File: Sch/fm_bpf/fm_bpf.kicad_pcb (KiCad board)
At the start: 2 copper layers, 28 parts, among them CN1 SMA_Edge, CN2 SMA_Edge, J1 JP2, U1 LP5907_SOT-23, U2 PSA4-5043+

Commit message: PCB layout in progress
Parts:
- removed J1: JP2, adc_lib:M20-9980245
- added W1: TEST_1P, adc_lib:68000-401HLF, F.Cu at (147.2, 92.5)
- added W2: TEST_1P, adc_lib:68000-401HLF, F.Cu at (144.4, 96.6)
- moved R2 8.09 mm to (143.7, 90.4), turned to 180 degrees
- moved U1 7.90 mm to (141.6, 92.5)
- moved C4 7.73 mm to (139.4, 94.4)
- moved C6 5.51 mm to (139.4, 95.6)
- moved L3 5.48 mm to (140.1, 97.9)
- moved C1 5.30 mm to (144.3, 92.8), turned to 90 degrees
- moved R1 5.07 mm to (138.4, 97.7)
- moved L4 4.74 mm to (140.0, 101.9)
- moved C8 4.55 mm to (139.3, 99.9)
- moved C13 3.36 mm to (150.1, 101.5)
- moved L7 2.01 mm to (149.0, 102.6)
- moved C12 1.84 mm to (147.1, 103.3)
- moved C14 1.72 mm to (151.8, 103.2)
- moved L6 1.54 mm to (145.9, 103.3)
- moved CN2 1.45 mm to (156.7, 102.6)
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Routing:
- net +5V: track 0.00 -> 13.3 mm
- net Net-(C12-Pad2): track 0.00 -> 4.99 mm
- net Net-(C13-Pad1): track 0.00 -> 4.41 mm
- net Net-(C4-Pad1): track 0.00 -> 4.23 mm
- net Net-(C5-Pad2): track 0.00 -> 2.97 mm
- net Net-(C8-Pad1): track 0.00 -> 2.35 mm
- net Net-(C14-Pad2): track 0.00 -> 1.66 mm
- net Net-(R2-Pad2): track 0.00 -> 1.17 mm
- net Net-(C10-Pad1): track 0.00 -> 1.09 mm
- net Net-(C3-Pad1): track 0.00 -> 1.03 mm
- net Net-(C11-Pad2): track 0.00 -> 1.00 mm
- net Net-(C7-Pad2): track 0.00 -> 0.88 mm
- added copper zone on F.Cu, net +5V
- added copper zone on B.Cu, net GND
- added copper zone on F.Cu, net GND
- added copper zone on F.Cu, net Net-(C4-Pad1)
- added copper zone on F.Cu, net Net-(C8-Pad1)

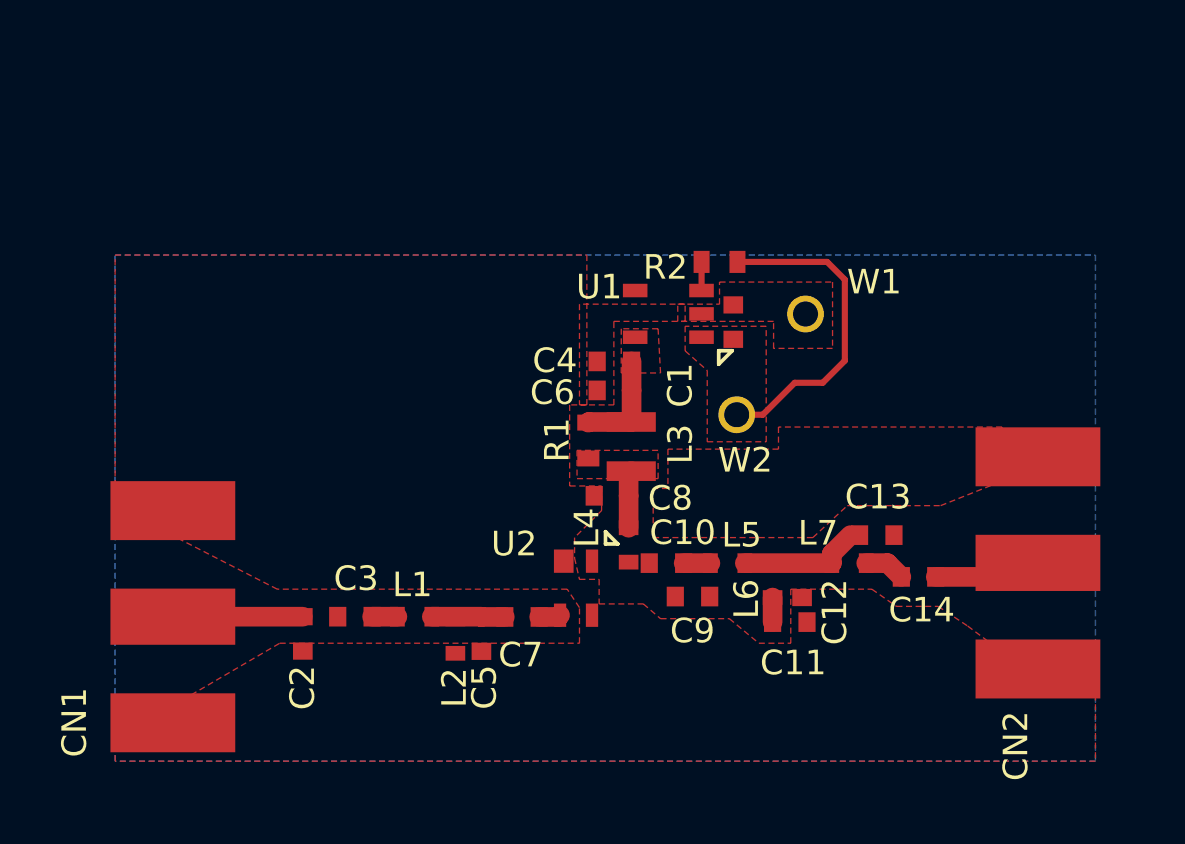
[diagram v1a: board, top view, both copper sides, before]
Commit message: FM BPF layout almost done
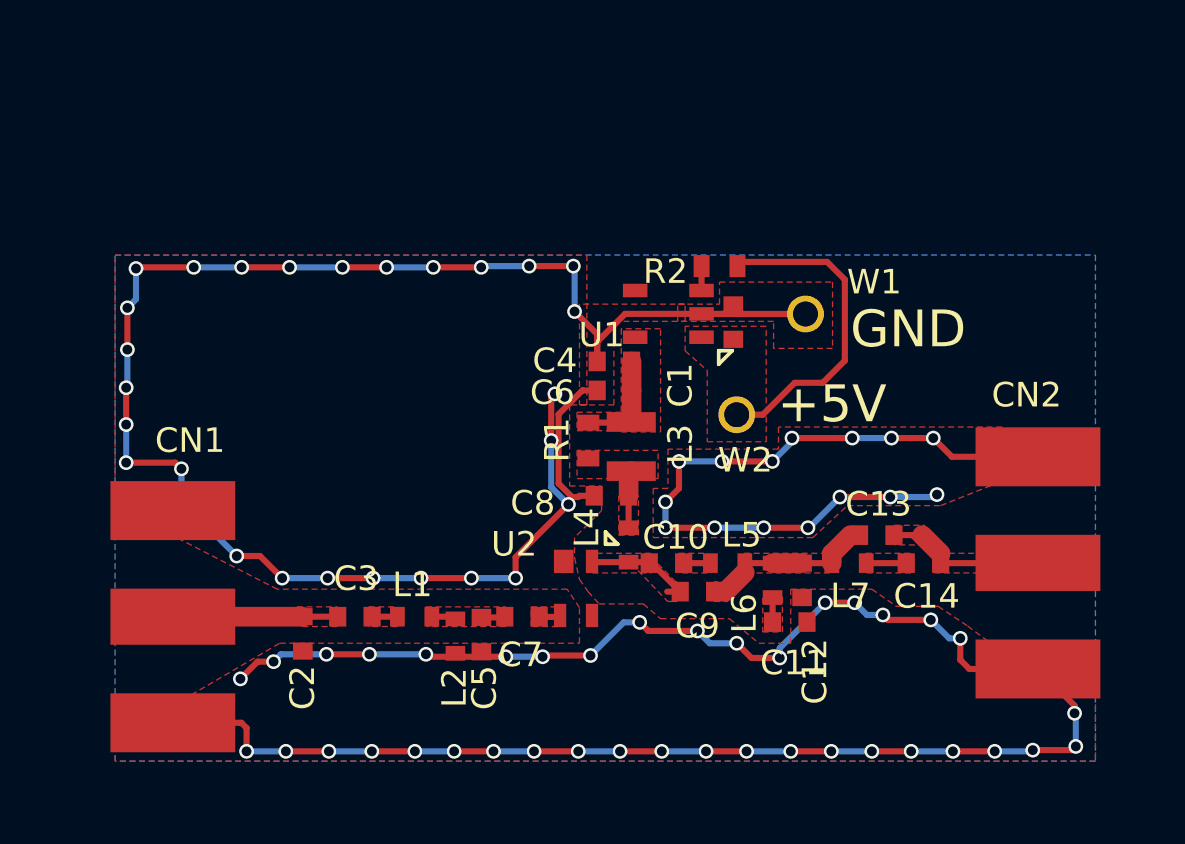
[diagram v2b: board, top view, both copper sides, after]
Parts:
- moved C14 0.59 mm to (152.0, 102.6)
- moved C9 0.28 mm to (142.8, 103.8)
- moved R2 0.17 mm to (143.7, 90.5)
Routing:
- net GND: track 0.00 -> 187.0 mm, vias 0 -> 81
- net Net-(C10-Pad2): track 0.00 -> 4.63 mm
- net Net-(C12-Pad2): track 4.99 -> 9.42 mm
- net Net-(C13-Pad1): track 4.41 -> 8.23 mm
- net Net-(C2-Pad1): track 5.29 -> 6.71 mm
- net Net-(C5-Pad2): track 2.97 -> 1.96 mm
- added copper zone on F.Cu, net Net-(C10-Pad1)
- added copper zone on F.Cu, net Net-(C10-Pad2)
- added copper zone on F.Cu, net Net-(C11-Pad2)
- added copper zone on F.Cu, net Net-(C12-Pad2)
- added copper zone on F.Cu, net Net-(C13-Pad1)
- added copper zone on F.Cu, net Net-(C14-Pad2)
- added copper zone on F.Cu, net Net-(C2-Pad1)
- added copper zone on F.Cu, net Net-(C3-Pad1)
- added copper zone on F.Cu, net Net-(C5-Pad2)
- added copper zone on F.Cu, net Net-(C7-Pad2)
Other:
- board text added: "+5V"
- board text added: "GND"

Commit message: add BPF cuts
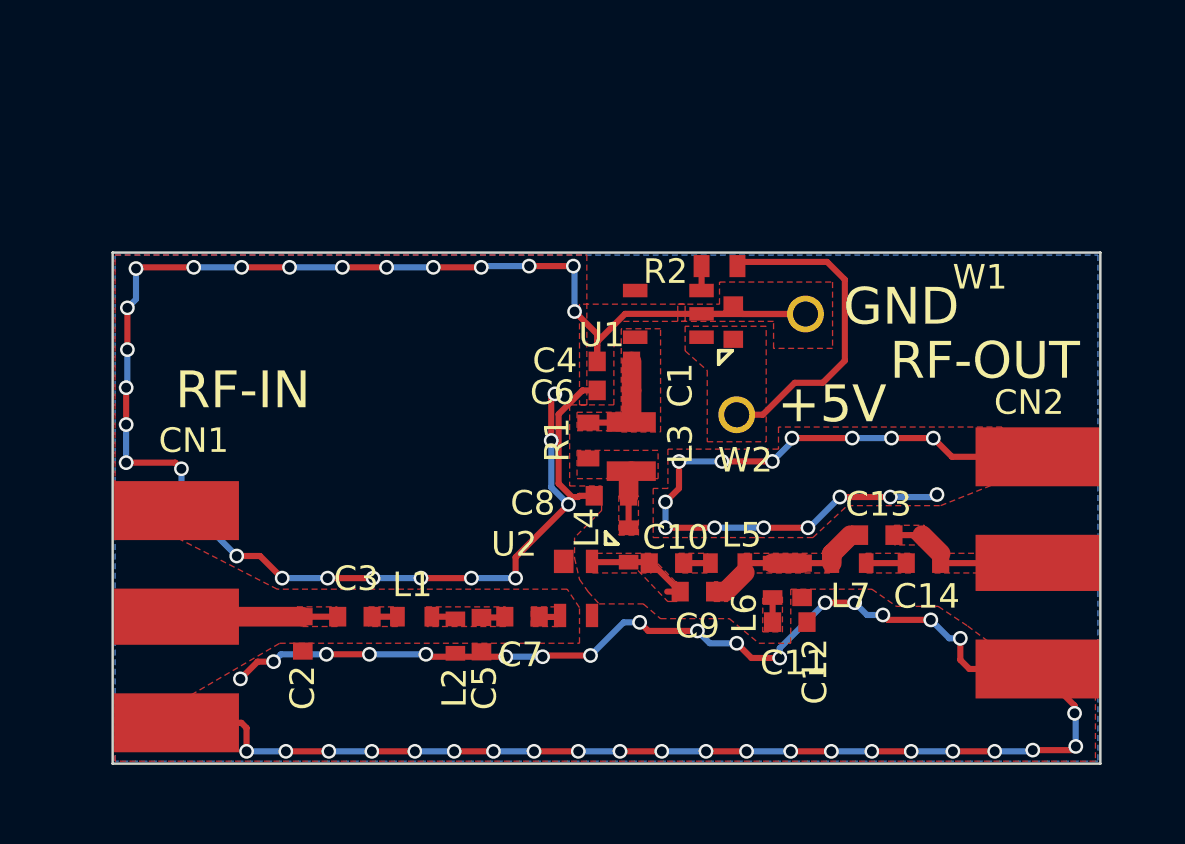
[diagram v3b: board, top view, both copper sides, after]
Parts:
- moved CN1 0.15 mm to (121.6, 104.8)
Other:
- board outline added: 40.2 x 20.8 mm
- board text added: "RF-IN"
- board text added: "RF-OUT"
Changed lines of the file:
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@@
     (links 47)
     (no_connects 0)
-    (area 116.475 89.525 159.4 115.952857)
+    (area 116.675 89.695 159.4 111.100002)
     (thickness 0.6)
-    (drawings 2)
+    (drawings 10)
     (tracks 273)
     (zones 0)
@@
     (pad_drill 0.6)
     (pad_to_mask_clearance 0)
-    (aux_axis_origin 0 0)
+    (aux_axis_origin 119 90)
     (visible_elements 7FFFFFFF)
     (pcbplotparams
@@
   )
   (module adc_lib:SMA_Edge (layer F.Cu)
-    (at 121.45 104.82 270)
+    (at 121.6 104.82 270)
     (fp_text reference CN1 (at -7.17 -0.7 360) (layer F.SilkS)
       (effects (font (size 1 1) (thickness 0.15)))
@@
   (module adc_lib:SMA_Edge (layer F.Cu)
     (at 156.66 102.63 270)
-    (fp_text reference CN2 (at -6.83 0.46 360) (layer F.SilkS)
+    (fp_text reference CN2 (at -6.53 0.36 360) (layer F.SilkS)
       (effects (font (size 1 1) (thickness 0.15)))
     )
@@
   (module adc_lib:68000-401HLF (layer F.Cu)
     (at 147.2 92.5)
-    (fp_text reference W1 (at 2.8 -1.3) (layer F.SilkS)
+    (fp_text reference W1 (at 7.1 -1.5) (layer F.SilkS)
       (effects (font (size 1 1) (thickness 0.15)))
     )
@@
       (net 1 +5V))
   )
+  (gr_text RF-OUT (at 154.5 94.4) (layer F.SilkS)
+    (effects (font (size 1.5 1.5) (thickness 0.3)))
+  )
+  (gr_text RF-IN (at 124.3 95.6) (layer F.SilkS)
+    (effects (font (size 1.5 1.5) (thickness 0.3)))
+  )
+  (dimension 20.8 (width 0.3) (layer Dwgs.User)
+    (gr_text "20.800 mm" (at 162.35 100.4 270) (layer Dwgs.User)
+      (effects (font (size 1.5 1.5) (thickness 0.3)))
+    )
+    (feature1 (pts (xy 160 110.8) (xy 163.7 110.8)))
+    (feature2 (pts (xy 160 90) (xy 163.7 90)))
+    (crossbar (pts (xy 161 90) (xy 161 110.8)))
+    (arrow1a (pts (xy 161 110.8) (xy 160.413579 109.673496)))
+    (arrow1b (pts (xy 161 110.8) (xy 161.586421 109.673496)))
+    (arrow2a (pts (xy 161 90) (xy 160.413579 91.126504)))
+    (arrow2b (pts (xy 161 90) (xy 161.586421 91.126504)))
+  )
+  (dimension 40.2 (width 0.3) (layer Dwgs.User)
+    (gr_text "40.200 mm" (at 139.1 86.15) (layer Dwgs.User)
+      (effects (font (size 1.5 1.5) (thickness 0.3)))
+    )
+    (feature1 (pts (xy 159.2 89) (xy 159.2 84.8)))
+    (feature2 (pts (xy 119 89) (xy 119 84.8)))
+    (crossbar (pts (xy 119 87.5) (xy 159.2 87.5)))
+    (arrow1a (pts (xy 159.2 87.5) (xy 158.073496 88.086421)))
+    (arrow1b (pts (xy 159.2 87.5) (xy 158.073496 86.913579)))
+    (arrow2a (pts (xy 119 87.5) (xy 120.126504 88.086421)))
+    (arrow2b (pts (xy 119 87.5) (xy 120.126504 86.913579)))
+  )
+  (gr_line (start 159.2 90) (end 119 90) (layer Edge.Cuts) (width 0.1))
+  (gr_line (start 159.2 110.8) (end 159.2 90) (layer Edge.Cuts) (width 0.1))
+  (gr_line (start 119 110.8) (end 159.2 110.8) (layer Edge.Cuts) (width 0.1))
+  (gr_line (start 119 90) (end 119 110.8) (layer Edge.Cuts) (width 0.1))
   (gr_text +5V (at 148.28 96.17) (layer F.SilkS)
     (effects (font (size 1.5 1.5) (thickness 0.3)))
   )
-  (gr_text GND (at 151.38 93.12) (layer F.SilkS)
+  (gr_text GND (at 151.1 92.2) (layer F.SilkS)
     (effects (font (size 1.5 1.5) (thickness 0.3)))
   )
@@
     (polygon
       (pts
-        (xy 159 110.7) (xy 119.1 110.7) (xy 119.1 90.1) (xy 159 90.1)
+        (xy 159.1 110.7) (xy 119.1 110.7) (xy 119.1 90.1) (xy 159.1 90.1)
       )
     )
